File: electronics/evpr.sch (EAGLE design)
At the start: 138 parts, among them J1 10118193-0001LF, Q1 AOD4184A, Q2 AOD4184A, T3 MMBT2222A, T5 MMBT2222A, U1 BQ2057TTS, U3 ESP32-WROOM-32D, U6 SN74AHCT125DR, U7 TPSM84824MOLR, U8 LTC4353CMSPBFMSOP-16_MS-M, X1 B3P-VH(LF)(SN), X2 BM02B-PASS-1-TFT(LF)(SN), X3 BM03B-PASS-1-TFT(LF)(SN), X4 BM03B-PASS-1-TFT(LF)(SN), X5 BM04B-PASS-1-TFT(LF)(SN)

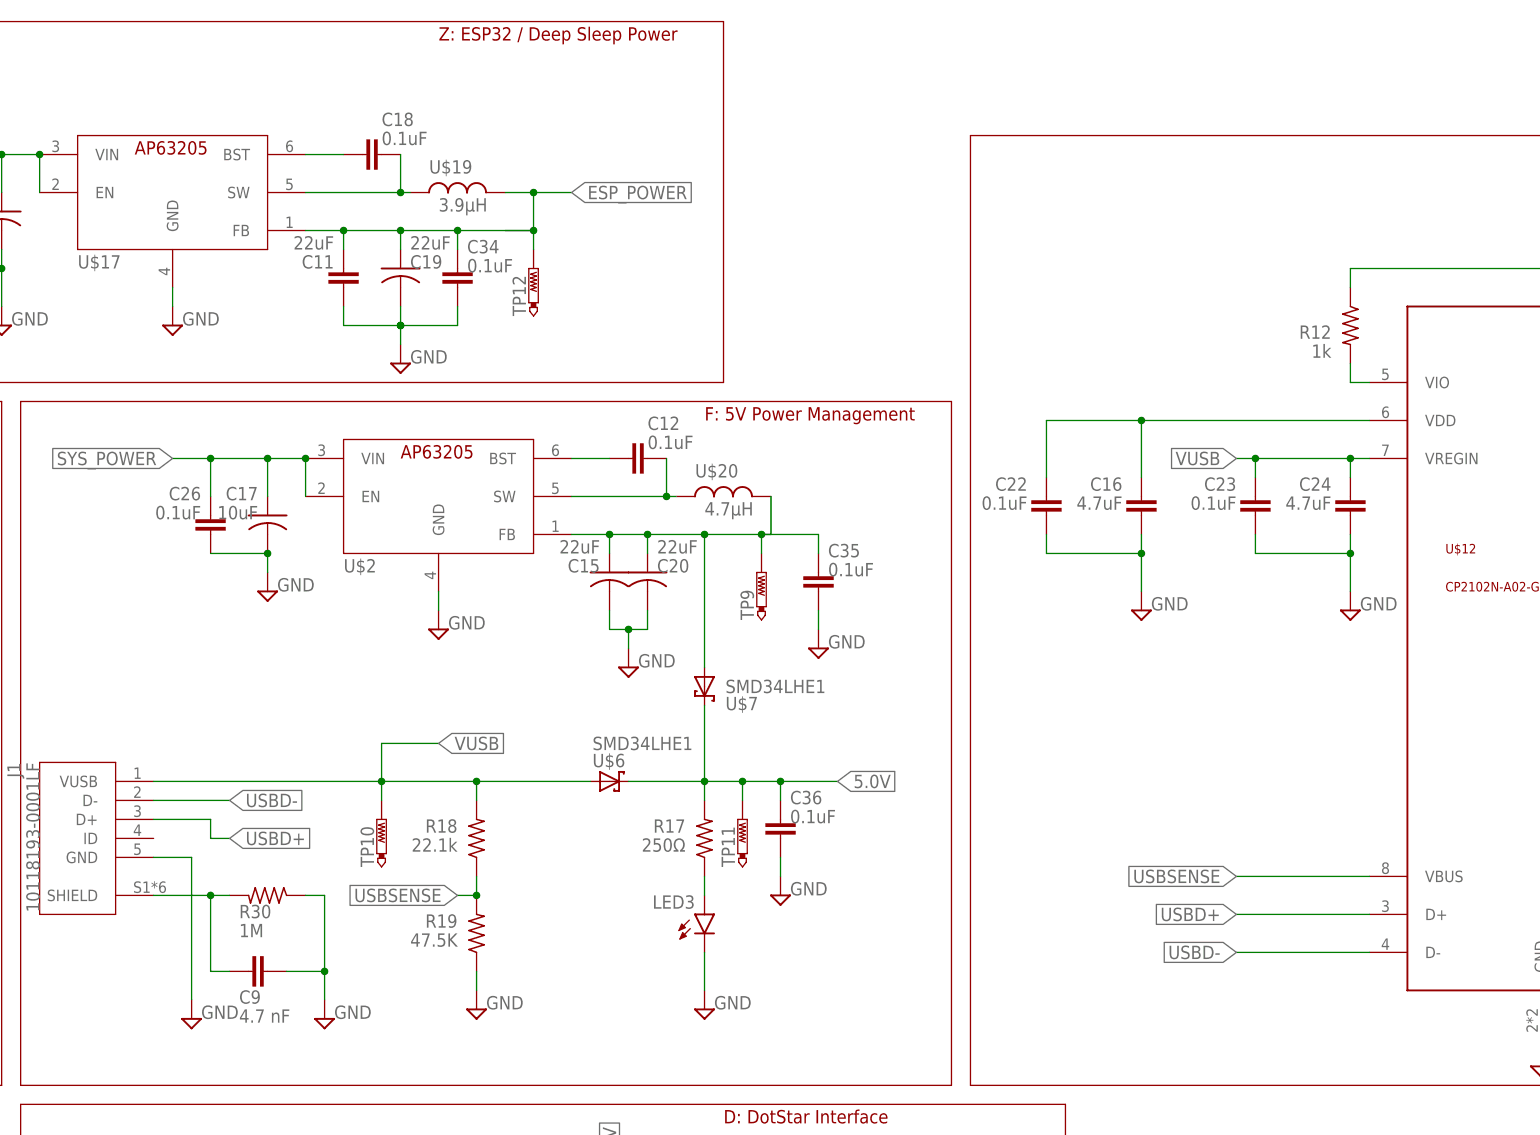
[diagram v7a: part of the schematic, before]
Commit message: Added testpoints; Reviewed all testpoints; Corrected 3.3V converter to AP63203
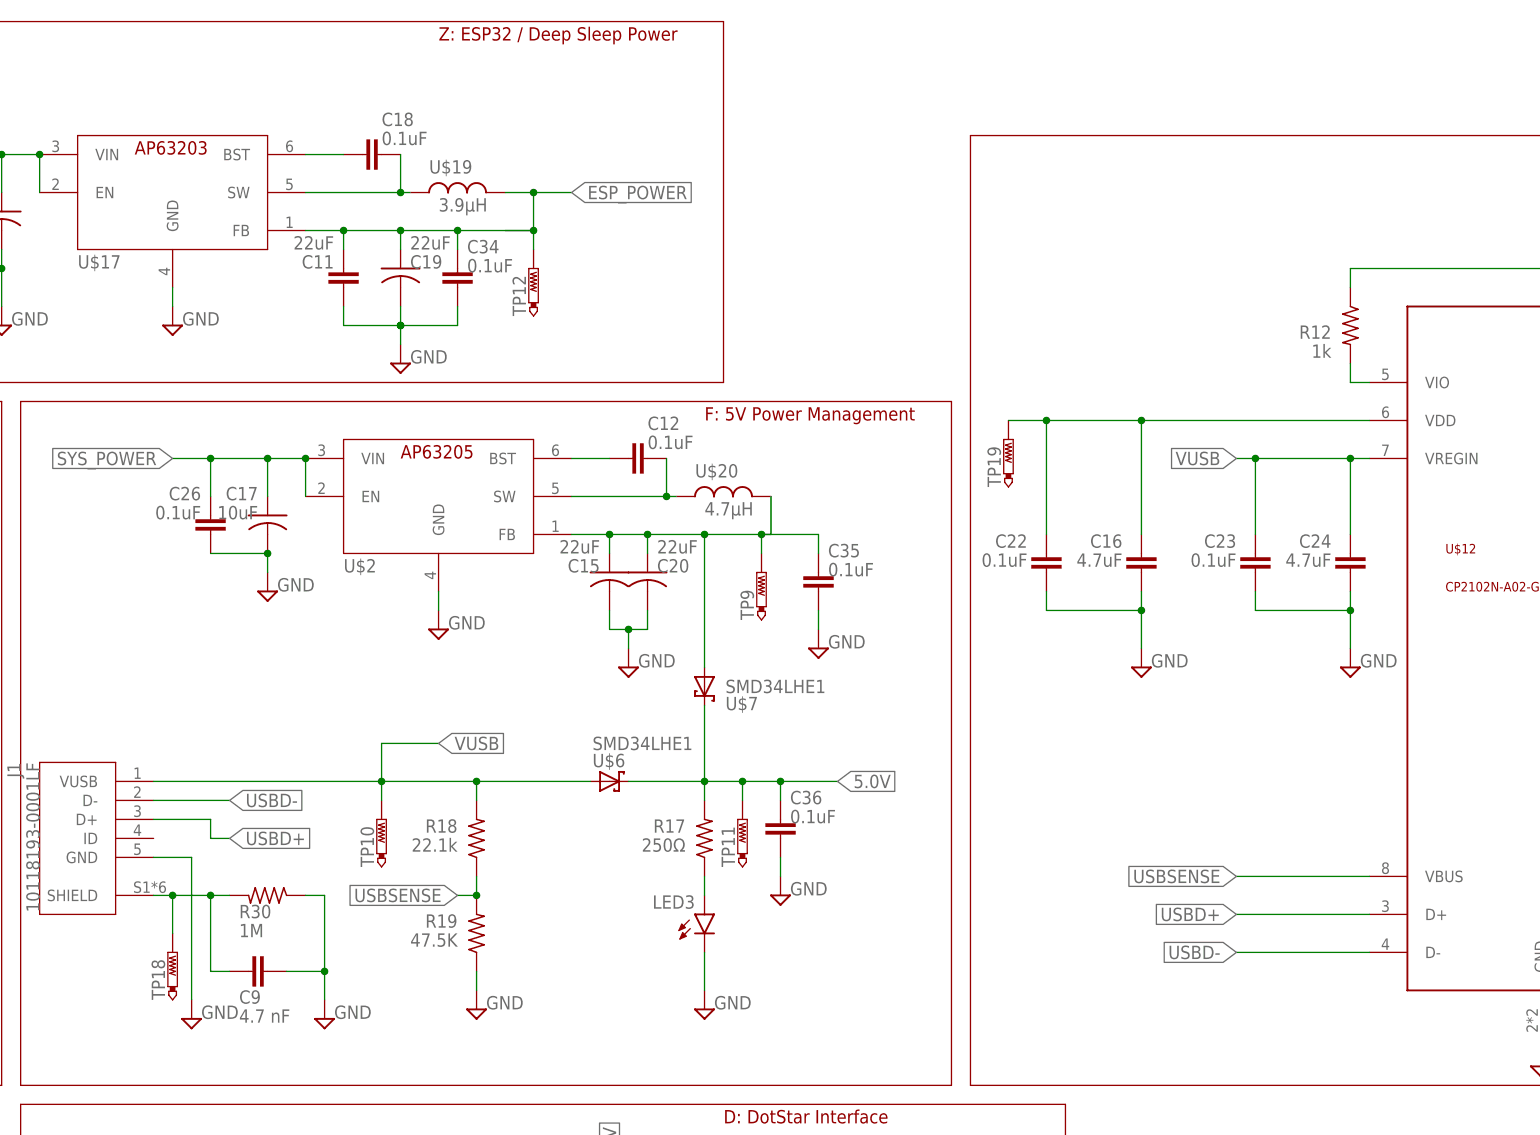
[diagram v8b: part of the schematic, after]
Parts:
- added TP18, TP19: PTR1TP10R, testpad:PTR1TP10R
- U$17: device mccloud:AP63205 -> mccloud:AP63203
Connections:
- net N$34: now also TP18.TP
- net N$40: now also TP19.TP
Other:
- moved on the sheet: C16, C22, C23, C24
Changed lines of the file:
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@@
 <attribute name="COMPONENT" value="GRM188R61A106KE69D"/>
 </part>
-<part name="U$17" library="mccloud" deviceset="AP63205" device="">
+<part name="U$17" library="mccloud" deviceset="AP63203" device="">
 <attribute name="COMPONENT" value="AP63205WU-7"/>
 </part>
@@
 <part name="SUPPLY52" library="supply2" library_urn="urn:adsk.eagle:library:372" deviceset="GND" device=""/>
 <part name="SUPPLY53" library="supply2" library_urn="urn:adsk.eagle:library:372" deviceset="GND" device=""/>
+<part name="TP18" library="testpad" library_urn="urn:adsk.eagle:library:385" deviceset="PTR1" device="TP10R" package3d_urn="urn:adsk.eagle:package:27959/1" value="PTR1TP10R"/>
+<part name="TP19" library="testpad" library_urn="urn:adsk.eagle:library:385" deviceset="PTR1" device="TP10R" package3d_urn="urn:adsk.eagle:package:27959/1" value="PTR1TP10R"/>
 </parts>
 <sheets>
@@
 <attribute name="COMPONENT" x="378.46" y="-48.26" size="1.778" layer="96" display="off"/>
 </instance>
-<instance part="SUPPLY17" gate="GND" x="281.94" y="-15.24" smashed="yes">
-<attribute name="VALUE" x="283.21" y="-15.24" size="1.778" layer="96"/>
+<instance part="SUPPLY17" gate="GND" x="281.94" y="-22.86" smashed="yes">
+<attribute name="VALUE" x="283.21" y="-22.86" size="1.778" layer="96"/>
 </instance>
 <instance part="LED2" gate="G$1" x="373.38" y="-2.54" smashed="yes">
@@
 <attribute name="VALUE" x="-250.19" y="-22.86" size="1.778" layer="96"/>
 </instance>
-<instance part="C22" gate="G$1" x="269.24" y="-2.54" smashed="yes" rot="R180">
-<attribute name="NAME" x="266.7" y="2.54" size="1.778" layer="95" rot="R180"/>
-<attribute name="VALUE" x="266.7" y="0" size="1.778" layer="96" rot="R180"/>
-<attribute name="COMPONENT" x="269.24" y="-2.54" size="1.778" layer="96" rot="R180" display="off"/>
-</instance>
-<instance part="C16" gate="G$1" x="281.94" y="-2.54" smashed="yes" rot="R180">
-<attribute name="NAME" x="279.4" y="2.54" size="1.778" layer="95" rot="R180"/>
-<attribute name="VALUE" x="279.4" y="0" size="1.778" layer="96" rot="R180"/>
-<attribute name="COMPONENT" x="281.94" y="-2.54" size="1.778" layer="96" rot="R180" display="off"/>
-</instance>
-<instance part="SUPPLY35" gate="GND" x="309.88" y="-15.24" smashed="yes">
-<attribute name="VALUE" x="311.15" y="-15.24" size="1.778" layer="96"/>
-</instance>
-<instance part="C23" gate="G$1" x="297.18" y="-2.54" smashed="yes" rot="R180">
-<attribute name="NAME" x="294.64" y="2.54" size="1.778" layer="95" rot="R180"/>
-<attribute name="VALUE" x="294.64" y="0" size="1.778" layer="96" rot="R180"/>
-<attribute name="COMPONENT" x="297.18" y="-2.54" size="1.778" layer="96" rot="R180" display="off"/>
-</instance>
-<instance part="C24" gate="G$1" x="309.88" y="-2.54" smashed="yes" rot="R180">
-<attribute name="NAME" x="307.34" y="2.54" size="1.778" layer="95" rot="R180"/>
-<attribute name="VALUE" x="307.34" y="0" size="1.778" layer="96" rot="R180"/>
-<attribute name="COMPONENT" x="309.88" y="-2.54" size="1.778" layer="96" rot="R180" display="off"/>
+<instance part="C22" gate="G$1" x="269.24" y="-10.16" smashed="yes" rot="R180">
+<attribute name="NAME" x="266.7" y="-5.08" size="1.778" layer="95" rot="R180"/>
+<attribute name="VALUE" x="266.7" y="-7.62" size="1.778" layer="96" rot="R180"/>
+<attribute name="COMPONENT" x="269.24" y="-10.16" size="1.778" layer="96" rot="R180" display="off"/>
+</instance>
+<instance part="C16" gate="G$1" x="281.94" y="-10.16" smashed="yes" rot="R180">
+<attribute name="NAME" x="279.4" y="-5.08" size="1.778" layer="95" rot="R180"/>
+<attribute name="VALUE" x="279.4" y="-7.62" size="1.778" layer="96" rot="R180"/>
+<attribute name="COMPONENT" x="281.94" y="-10.16" size="1.778" layer="96" rot="R180" display="off"/>
+</instance>
+<instance part="SUPPLY35" gate="GND" x="309.88" y="-22.86" smashed="yes">
+<attribute name="VALUE" x="311.15" y="-22.86" size="1.778" layer="96"/>
+</instance>
+<instance part="C23" gate="G$1" x="297.18" y="-10.16" smashed="yes" rot="R180">
+<attribute name="NAME" x="294.64" y="-5.08" size="1.778" layer="95" rot="R180"/>
+<attribute name="VALUE" x="294.64" y="-7.62" size="1.778" layer="96" rot="R180"/>
+<attribute name="COMPONENT" x="297.18" y="-10.16" size="1.778" layer="96" rot="R180" display="off"/>
+</instance>
+<instance part="C24" gate="G$1" x="309.88" y="-10.16" smashed="yes" rot="R180">
+<attribute name="NAME" x="307.34" y="-5.08" size="1.778" layer="95" rot="R180"/>
+<attribute name="VALUE" x="307.34" y="-7.62" size="1.778" layer="96" rot="R180"/>
+<attribute name="COMPONENT" x="309.88" y="-10.16" size="1.778" layer="96" rot="R180" display="off"/>
 </instance>
 <instance part="R7" gate="G$1" x="45.72" y="-15.24" smashed="yes" rot="R270">
@@
 <instance part="SUPPLY53" gate="GND" x="223.52" y="-137.16" smashed="yes">
 <attribute name="VALUE" x="224.79" y="-137.16" size="1.778" layer="96"/>
+</instance>
+<instance part="TP18" gate="G$1" x="152.4" y="-60.96" smashed="yes">
+<attribute name="NAME" x="151.384" y="-67.31" size="1.778" layer="95" rot="R90"/>
+<attribute name="TP_SIGNAL_NAME" x="153.67" y="-63.5" size="1.778" layer="97"/>
+</instance>
+<instance part="TP19" gate="G$1" x="264.16" y="7.62" smashed="yes">
+<attribute name="NAME" x="263.144" y="1.27" size="1.778" layer="95" rot="R90"/>
+<attribute name="TP_SIGNAL_NAME" x="265.43" y="5.08" size="1.778" layer="97"/>
 </instance>
 </instances>
@@
 <segment>
 <pinref part="SUPPLY17" gate="GND" pin="GND"/>
-<wire x1="281.94" y1="-12.7" x2="281.94" y2="-7.62" width="0.1524" layer="91"/>
+<wire x1="281.94" y1="-20.32" x2="281.94" y2="-15.24" width="0.1524" layer="91"/>
 <pinref part="C16" gate="G$1" pin="1"/>
 <pinref part="C22" gate="G$1" pin="1"/>
-<wire x1="281.94" y1="-7.62" x2="281.94" y2="-5.08" width="0.1524" layer="91"/>
-<wire x1="269.24" y1="-5.08" x2="269.24" y2="-7.62" width="0.1524" layer="91"/>
-<wire x1="269.24" y1="-7.62" x2="281.94" y2="-7.62" width="0.1524" layer="91"/>
-<junction x="281.94" y="-7.62"/>
+<wire x1="281.94" y1="-15.24" x2="281.94" y2="-12.7" width="0.1524" layer="91"/>
+<wire x1="269.24" y1="-12.7" x2="269.24" y2="-15.24" width="0.1524" layer="91"/>
+<wire x1="269.24" y1="-15.24" x2="281.94" y2="-15.24" width="0.1524" layer="91"/>
+<junction x="281.94" y="-15.24"/>
 </segment>
 <segment>
@@
 <segment>
 <pinref part="SUPPLY35" gate="GND" pin="GND"/>
-<wire x1="309.88" y1="-12.7" x2="309.88" y2="-7.62" width="0.1524" layer="91"/>
+<wire x1="309.88" y1="-20.32" x2="309.88" y2="-15.24" width="0.1524" layer="91"/>
 <pinref part="C24" gate="G$1" pin="1"/>
 <pinref part="C23" gate="G$1" pin="1"/>
-<wire x1="309.88" y1="-7.62" x2="309.88" y2="-5.08" width="0.1524" layer="91"/>
-<wire x1="297.18" y1="-5.08" x2="297.18" y2="-7.62" width="0.1524" layer="91"/>
-<wire x1="297.18" y1="-7.62" x2="309.88" y2="-7.62" width="0.1524" layer="91"/>
-<junction x="309.88" y="-7.62"/>
+<wire x1="309.88" y1="-15.24" x2="309.88" y2="-12.7" width="0.1524" layer="91"/>
+<wire x1="297.18" y1="-12.7" x2="297.18" y2="-15.24" width="0.1524" layer="91"/>
+<wire x1="297.18" y1="-15.24" x2="309.88" y2="-15.24" width="0.1524" layer="91"/>
+<junction x="309.88" y="-15.24"/>
 </segment>
 <segment>
@@
 <pinref part="U$12" gate="A" pin="VREGIN"/>
 <pinref part="C24" gate="G$1" pin="2"/>
-<wire x1="309.88" y1="2.54" x2="309.88" y2="5.08" width="0.1524" layer="91"/>
+<wire x1="309.88" y1="-5.08" x2="309.88" y2="5.08" width="0.1524" layer="91"/>
 <wire x1="309.88" y1="5.08" x2="312.42" y2="5.08" width="0.1524" layer="91"/>
 <pinref part="C23" gate="G$1" pin="2"/>
-<wire x1="297.18" y1="2.54" x2="297.18" y2="5.08" width="0.1524" layer="91"/>
+<wire x1="297.18" y1="-5.08" x2="297.18" y2="5.08" width="0.1524" layer="91"/>
 <wire x1="297.18" y1="5.08" x2="309.88" y2="5.08" width="0.1524" layer="91"/>
 <junction x="309.88" y="5.08"/>
@@
 <pinref part="R30" gate="G$1" pin="2"/>
 <pinref part="J1" gate="G$1" pin="SHIELD"/>
-<wire x1="149.86" y1="-53.34" x2="157.48" y2="-53.34" width="0.1524" layer="91"/>
+<wire x1="149.86" y1="-53.34" x2="152.4" y2="-53.34" width="0.1524" layer="91"/>
 <pinref part="C9" gate="G$1" pin="2"/>
+<wire x1="152.4" y1="-53.34" x2="157.48" y2="-53.34" width="0.1524" layer="91"/>
 <wire x1="157.48" y1="-53.34" x2="160.02" y2="-53.34" width="0.1524" layer="91"/>
 <wire x1="160.02" y1="-63.5" x2="157.48" y2="-63.5" width="0.1524" layer="91"/>
 <wire x1="157.48" y1="-63.5" x2="157.48" y2="-53.34" width="0.1524" layer="91"/>
 <junction x="157.48" y="-53.34"/>
+<pinref part="TP18" gate="G$1" pin="TP"/>
+<wire x1="152.4" y1="-58.42" x2="152.4" y2="-53.34" width="0.1524" layer="91"/>
+<junction x="152.4" y="-53.34"/>
 </segment>
 </net>
@@
 <pinref part="U$12" gate="A" pin="VDD"/>
 <wire x1="312.42" y1="10.16" x2="281.94" y2="10.16" width="0.1524" layer="91"/>
-<wire x1="281.94" y1="10.16" x2="281.94" y2="2.54" width="0.1524" layer="91"/>
+<wire x1="281.94" y1="10.16" x2="281.94" y2="-5.08" width="0.1524" layer="91"/>
 <pinref part="C16" gate="G$1" pin="2"/>
 <pinref part="C22" gate="G$1" pin="2"/>
-<wire x1="269.24" y1="2.54" x2="269.24" y2="10.16" width="0.1524" layer="91"/>
+<wire x1="269.24" y1="-5.08" x2="269.24" y2="10.16" width="0.1524" layer="91"/>
 <wire x1="269.24" y1="10.16" x2="281.94" y2="10.16" width="0.1524" layer="91"/>
 <junction x="281.94" y="10.16"/>
-</segment>
-</net>
+<pinref part="TP19" gate="G$1" pin="TP"/>
+<wire x1="264.16" y1="10.16" x2="269.24" y2="10.16" width="0.1524" layer="91"/>
+<junction x="269.24" y="10.16"/>
+</segment>
+</net>
